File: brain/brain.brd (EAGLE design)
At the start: 59.7 x 53.3 mm, 7 parts

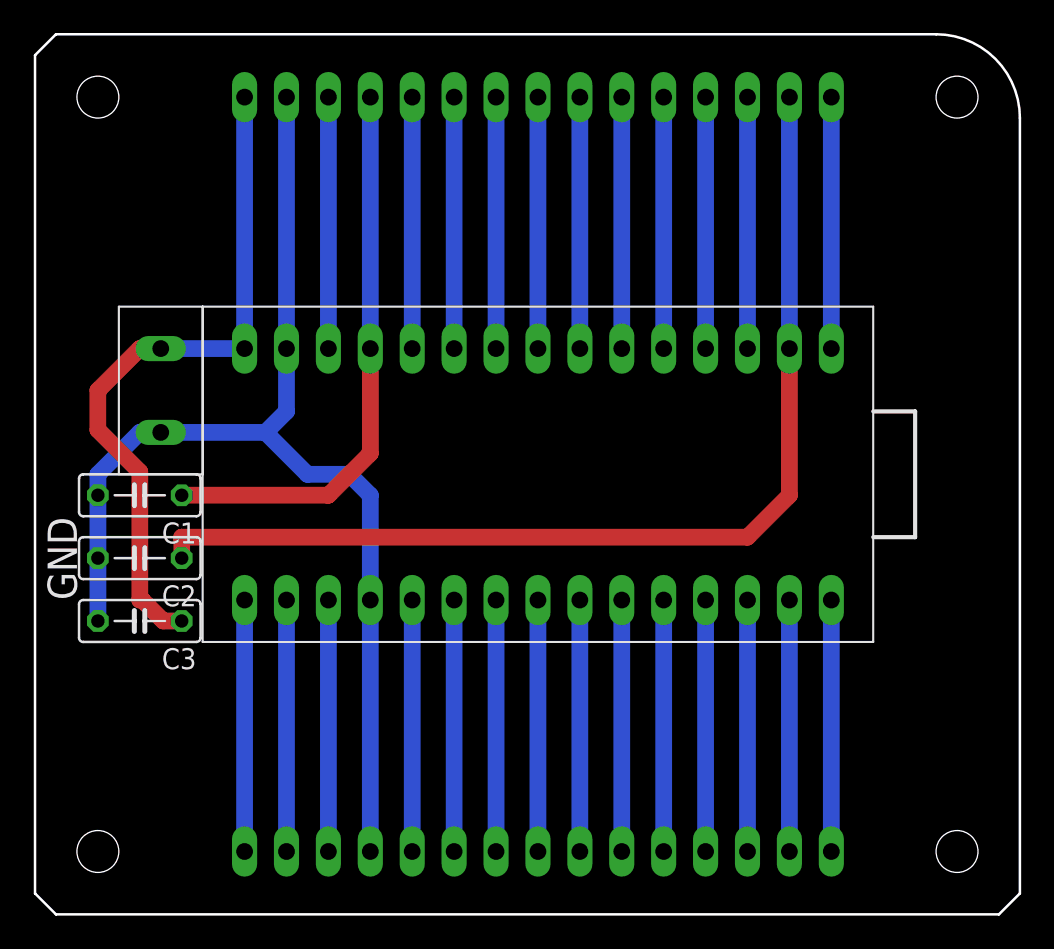
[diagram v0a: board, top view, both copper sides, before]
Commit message: On brain board: Added holes for strain relief of power cables. Added silkscreen to indicate ground and different power pins on Nano. Added silkscreen denoting the board. Added silkscreen to mark positive and negative terminals of power input.
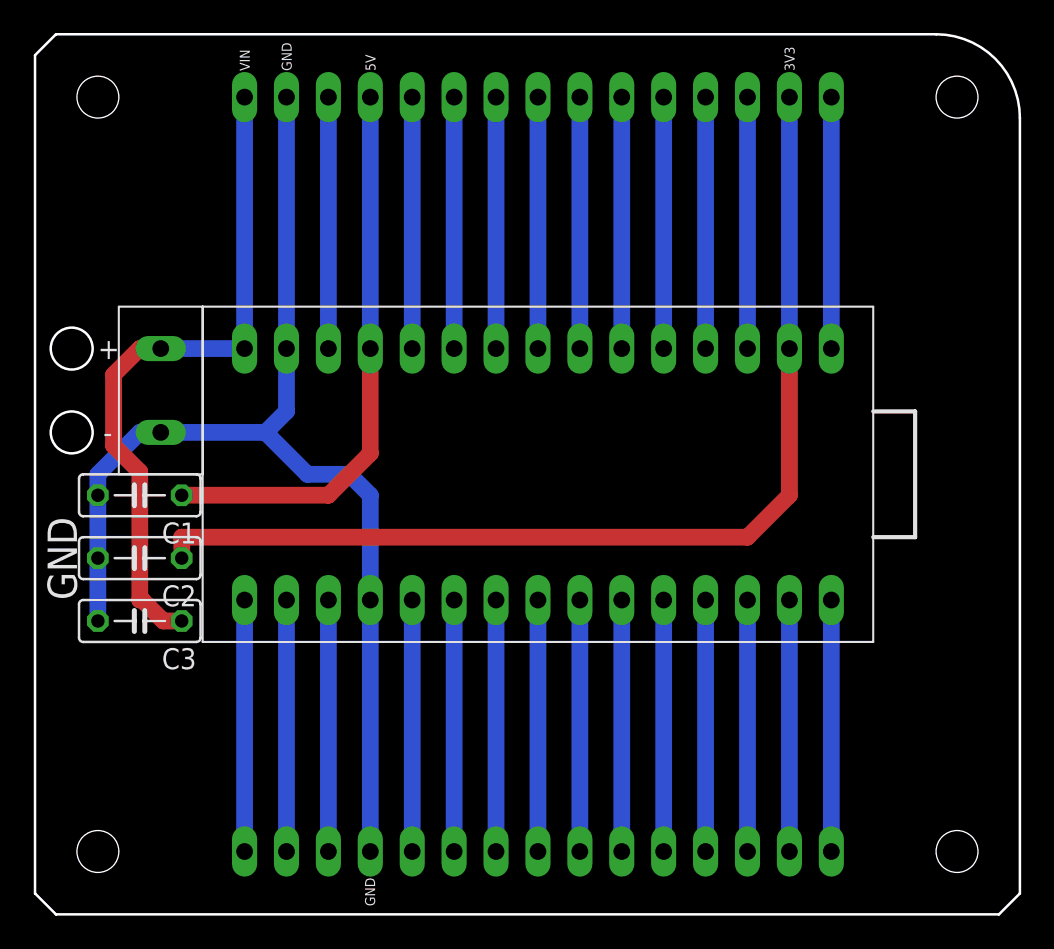
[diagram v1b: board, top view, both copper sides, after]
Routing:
- net V+: track 42.0 -> 41.2 mm
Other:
- outline, holes or cut-outs redrawn
- board text added: "+"
- board text added: "-"
- board text added: "3V3"
- board text added: "5V"
- board text added: "RC CARS BRAIN BOARD NANO EDITION"
- board text added: "VIN"
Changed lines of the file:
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@@
 <setting verticaltext="up"/>
 </settings>
-<grid distance="50" unitdist="mil" unit="mil" style="lines" multiple="1" display="yes" altdistance="5" altunitdist="mil" altunit="mil"/>
+<grid distance="12.5" unitdist="mil" unit="mil" style="lines" multiple="1" display="yes" altdistance="5" altunitdist="mil" altunit="mil"/>
 <layers>
 <layer number="1" name="Top" color="4" fill="1" visible="yes" active="yes"/>
@@
 <wire x1="53.34" y1="30.48" x2="53.34" y2="22.86" width="0.254" layer="21"/>
 <wire x1="53.34" y1="22.86" x2="50.8" y2="22.86" width="0.254" layer="21"/>
+<circle x="2.2225" y="34.29" radius="1.27" width="0.1524" layer="20"/>
+<circle x="2.2225" y="29.21" radius="1.27" width="0.1524" layer="20"/>
+<text x="13.0175" y="51.1175" size="0.6096" layer="21" rot="R90">VIN</text>
+<text x="15.5575" y="51.1175" size="0.6096" layer="21" rot="R90">GND</text>
+<text x="20.6375" y="51.1175" size="0.6096" layer="21" rot="R90">5V</text>
+<text x="46.0375" y="51.1175" size="0.6096" layer="21" rot="R90">3V3</text>
+<text x="20.0025" y="2.2225" size="0.6096" layer="21" rot="R270">GND</text>
+<text x="44.7675" y="24.765" size="1.778" layer="22" rot="MR0">RC CARS BRAIN BOARD
+NANO EDITION</text>
+<text x="3.81" y="33.655" size="1.27" layer="21">+</text>
+<text x="4.1275" y="28.575" size="1.27" layer="21">-</text>
 </plain>
 <attributes>
@@
 <wire x1="7.7724" y1="17.78" x2="6.5024" y2="19.05" width="1.016" layer="1"/>
 <wire x1="6.5024" y1="19.05" x2="6.35" y2="19.05" width="1.016" layer="1"/>
-<wire x1="6.35" y1="26.8224" x2="3.81" y2="29.3624" width="1.016" layer="1"/>
-<wire x1="3.81" y1="29.3624" x2="3.81" y2="31.75" width="1.016" layer="1"/>
-<wire x1="3.81" y1="31.75" x2="6.35" y2="34.29" width="1.016" layer="1"/>
+<wire x1="6.35" y1="26.8224" x2="4.7625" y2="28.4099" width="1.016" layer="1"/>
+<wire x1="4.7625" y1="28.4099" x2="4.7625" y2="32.7025" width="1.016" layer="1"/>
+<wire x1="4.7625" y1="32.7025" x2="6.35" y2="34.29" width="1.016" layer="1"/>
 <wire x1="6.35" y1="34.29" x2="7.62" y2="34.29" width="1.016" layer="1"/>
 <wire x1="6.35" y1="19.05" x2="6.35" y2="26.8224" width="1.016" layer="1"/>
@@
 </drawing>
 <compatibility>
+<note version="6.3" minversion="6.2.2" severity="warning">
+Since Version 6.2.2 text objects can contain more than one line,
+which will not be processed correctly with this version.
+</note>
 <note version="8.2" severity="warning">
 Since Version 8.2, EAGLE supports online libraries. The ids

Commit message: Added breadboard board. This commit is going to production.
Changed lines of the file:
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@@
 <?xml version="1.0" encoding="utf-8"?>
 <!DOCTYPE eagle SYSTEM "eagle.dtd">
-<eagle version="9.6.2">
+<eagle version="9.7.0">
 <drawing>
 <settings>
@@
 <setting verticaltext="up"/>
 </settings>
-<grid distance="12.5" unitdist="mil" unit="mil" style="lines" multiple="1" display="yes" altdistance="5" altunitdist="mil" altunit="mil"/>
+<grid distance="50" unitdist="mil" unit="mil" style="lines" multiple="1" display="yes" altdistance="5" altunitdist="mil" altunit="mil"/>
 <layers>
 <layer number="1" name="Top" color="4" fill="1" visible="yes" active="yes"/>
@@
 <text x="3.81" y="33.655" size="1.27" layer="21">+</text>
 <text x="4.1275" y="28.575" size="1.27" layer="21">-</text>
+<rectangle x1="50.8" y1="44.45" x2="59.69" y2="53.34" layer="21"/>
+<rectangle x1="50.8" y1="44.45" x2="59.69" y2="53.34" layer="22"/>
 </plain>
 <attributes>
